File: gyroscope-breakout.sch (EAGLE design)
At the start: 9 parts, among them U2 L3GD20H, U3 MIC5504-3.3YM5-T5

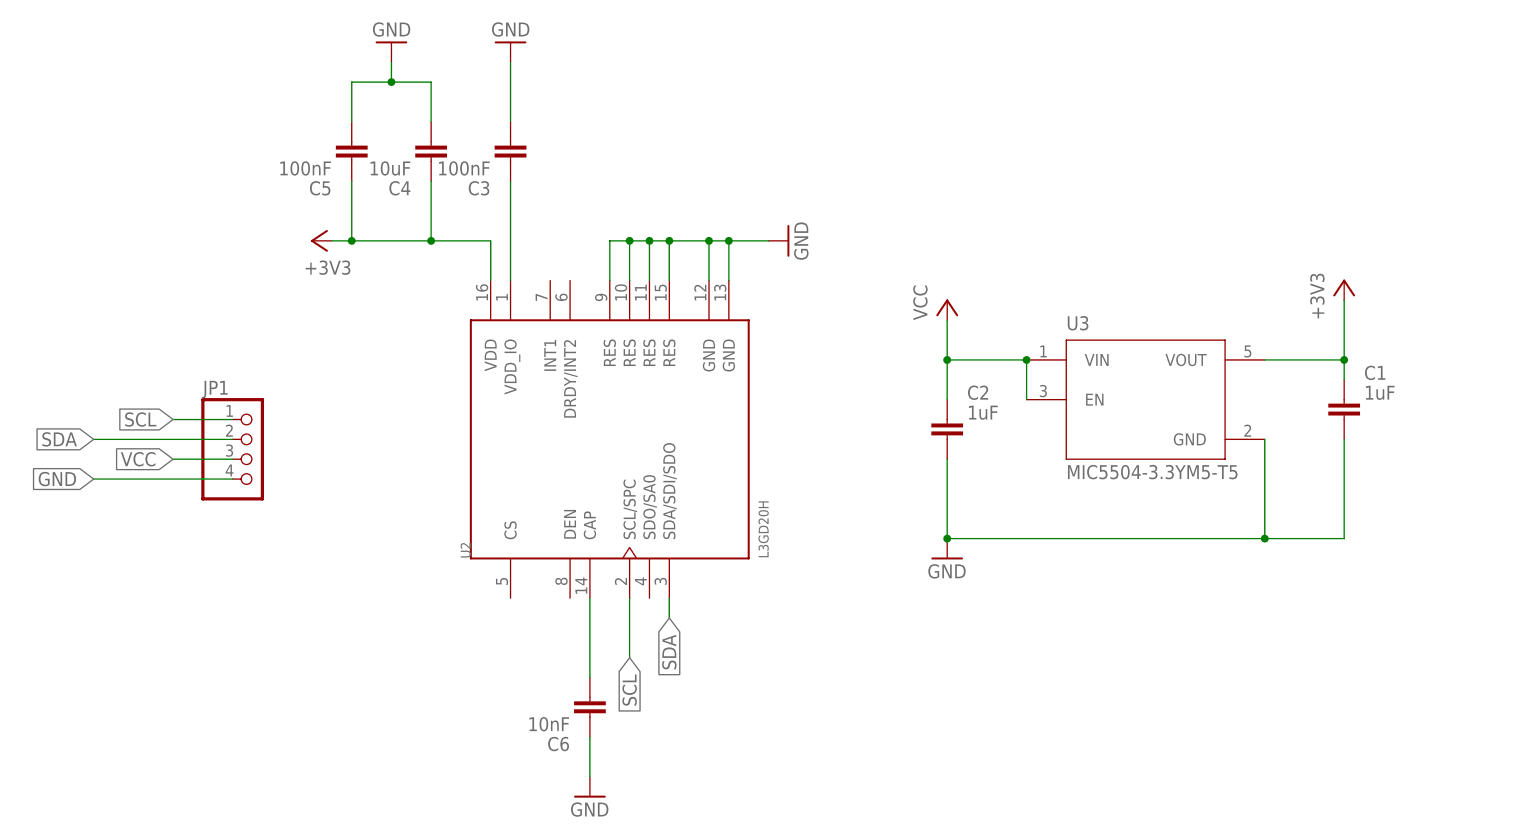
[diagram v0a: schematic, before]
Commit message: fix gyro connections
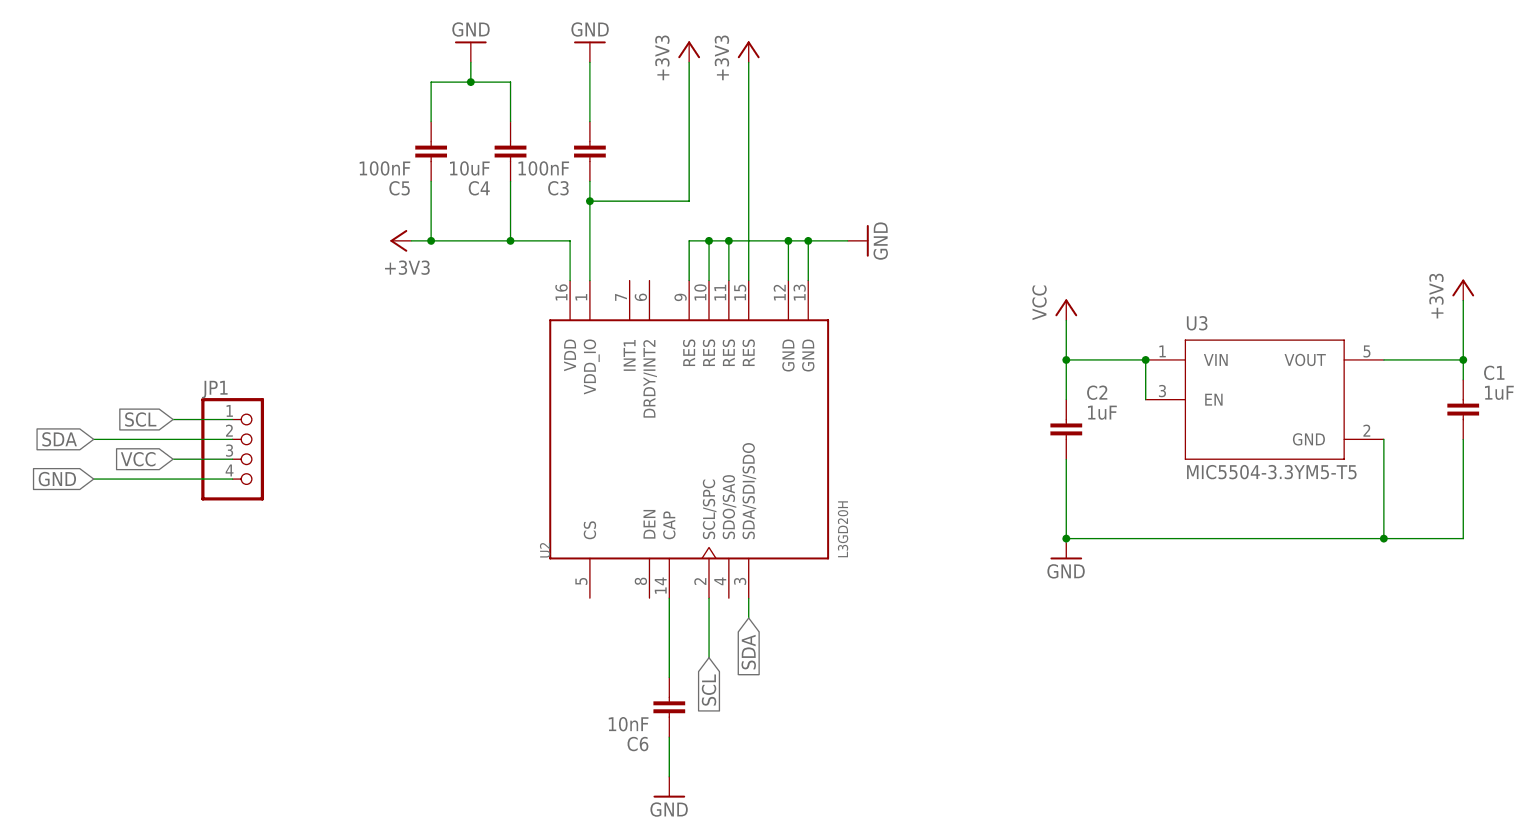
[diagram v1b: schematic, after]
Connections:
- removed net N$2: C3.1, U2.VDD_IO
- net +3V3: now also C3.1, U2.RES@4, U2.VDD_IO
- net GND: no longer U2.RES@4
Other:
- moved on the sheet: C1, C2, C3, C4, C5, C6, U2, U3
